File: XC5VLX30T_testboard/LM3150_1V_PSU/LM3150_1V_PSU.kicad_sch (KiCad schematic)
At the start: 14 parts, among them Q1 STP40NF03L, Q2 STP40NF03L, U1 LM3150MHX/NOPB

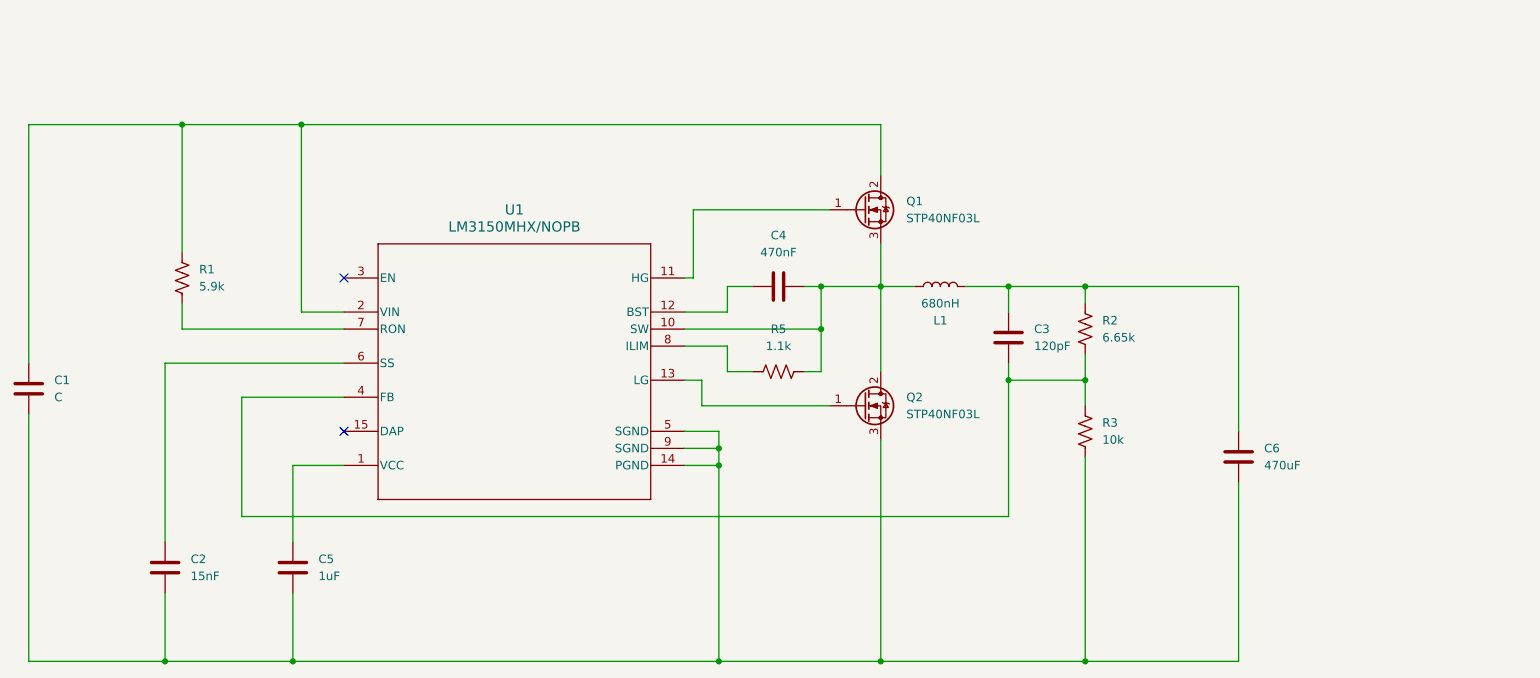
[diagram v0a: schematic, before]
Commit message: lm3150 psu
alternate psu using lm3150
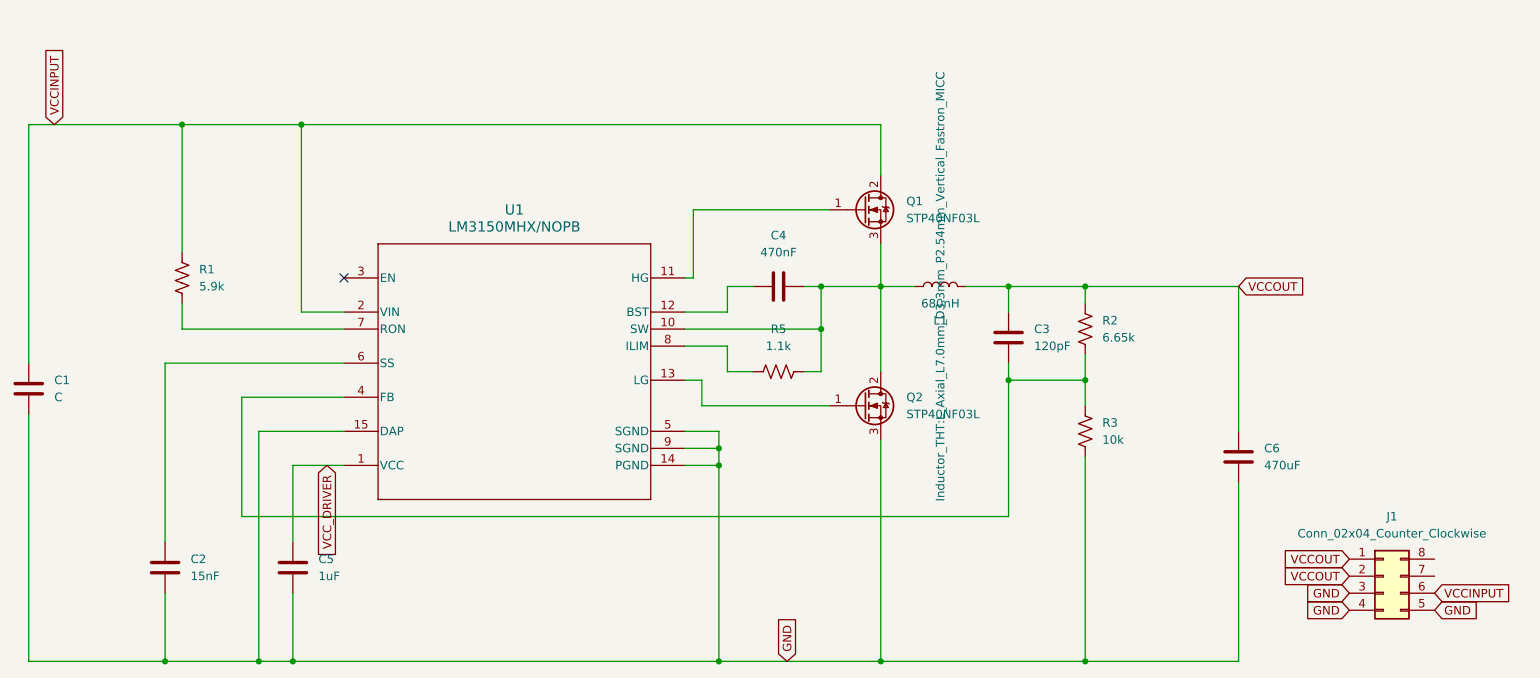
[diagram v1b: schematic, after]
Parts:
- added J1: Conn_02x04_Counter_Clockwise, virtex5_buck_footprint:virtex5_buck, symbol Connector_Generic:Conn_02x04_Counter_Clockwise
- C1: footprint (none) -> Capacitor_THT:C_Disc_D3.0mm_W2.0mm_P2.50mm
- C2, C3, C4, C5, C6: footprint (none) -> Capacitor_THT:C_Disc_D3.0mm_W1.6mm_P2.50mm
- L1: footprint (none) -> Inductor_THT:L_Axial_L7.0mm_D3.3mm_P2.54mm_Vertical_Fastron_MICC
- R1, R2, R3, R5: footprint (none) -> Resistor_THT:R_Axial_DIN0204_L3.6mm_D1.6mm_P5.08mm_Horizontal
- U1: footprint MXA14A -> Package_SO:HTSSOP-14-1EP_4.4x5mm_P0.65mm_EP3.4x5mm_Mask3x3.1mm_ThermalVias
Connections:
- net VCC_DRIVER: now reaches C5.1, U1.1 (VCC)
- net GND: now reaches C1.2, C2.2, C5.2, C6.2, Q2.3 (S), R3.2, U1.14 (PGND), U1.5 (SGND), U1.9 (SGND)
- net GND: now also U1.15 (DAP), J1.3 (Pin_3), J1.4 (Pin_4), J1.5 (Pin_5)
- net VCCINPUT: now reaches C1.1, Q1.2 (D), R1.1, U1.2 (VIN)
- net VCCINPUT: now also J1.6 (Pin_6)
- net VCCOUT: now reaches C3.1, C6.1, L1.1, R2.1
- net VCCOUT: now also J1.1 (Pin_1), J1.2 (Pin_2)
- no-connect marks 2 -> 1
